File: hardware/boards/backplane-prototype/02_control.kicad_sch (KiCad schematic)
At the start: 13 parts, among them J10 TC2030-IDC-NL SWD, U1 STM32C092GCU6

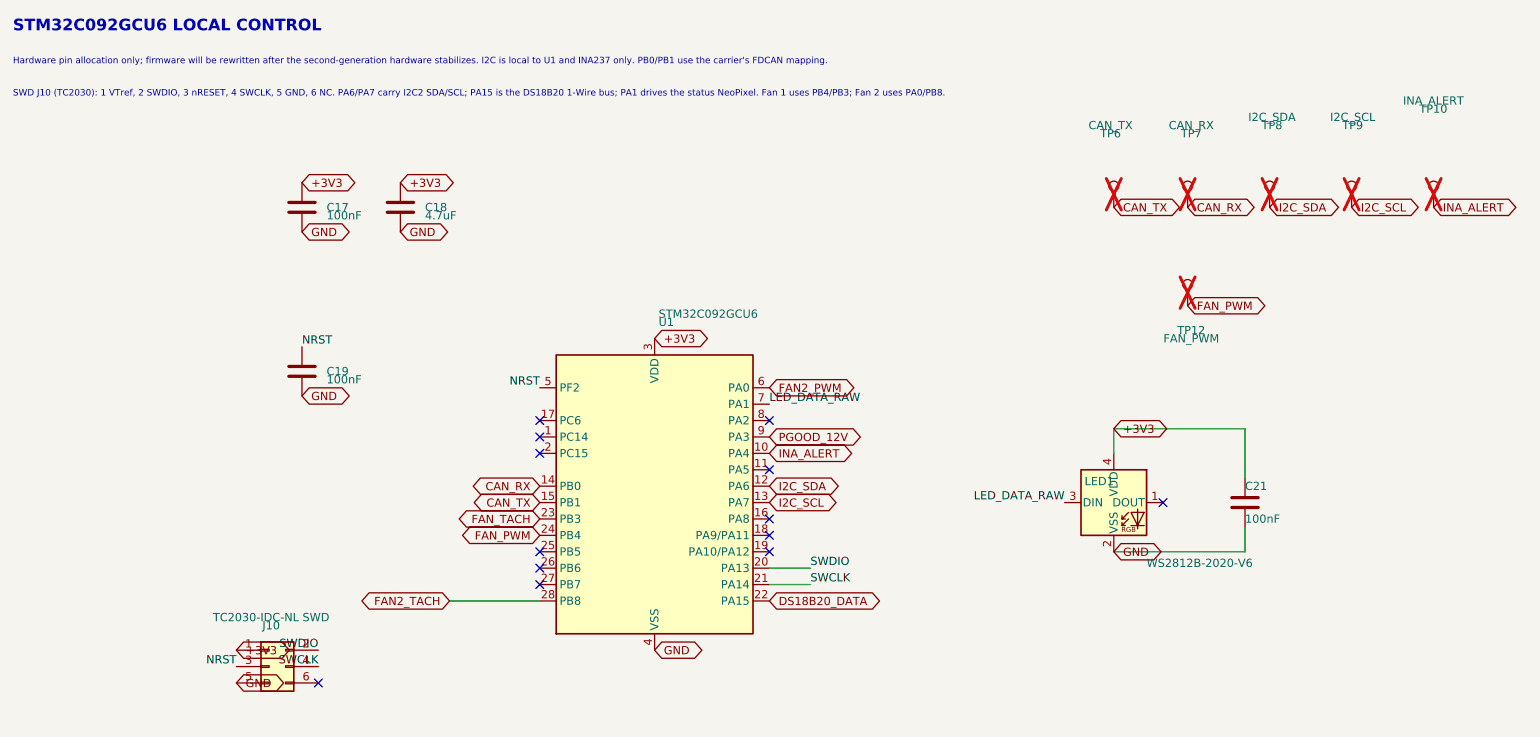
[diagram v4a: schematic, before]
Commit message: move fan1 signals off TIM3 pins
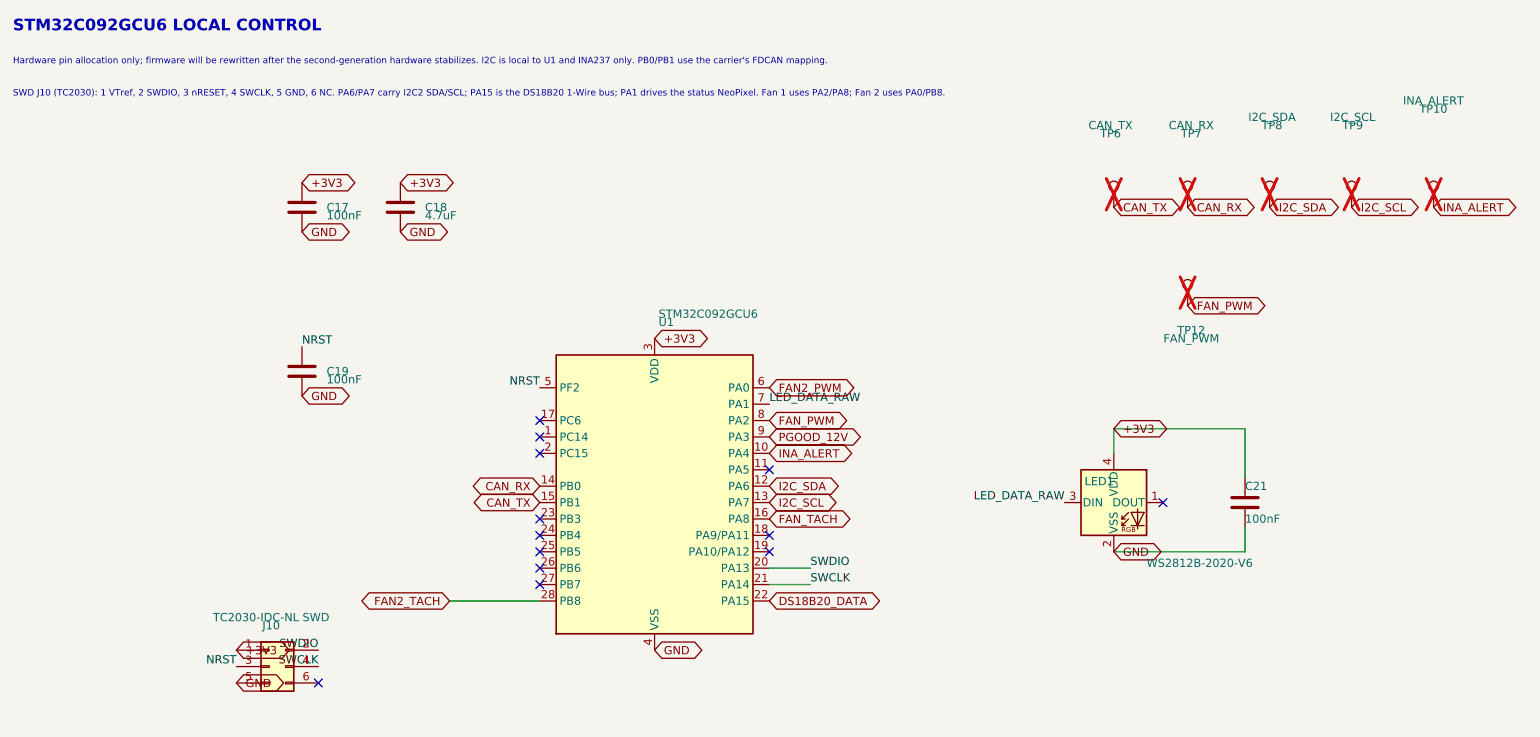
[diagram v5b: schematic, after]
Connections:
- net FAN_PWM: now also U1.8 (PA2); no longer U1.24 (PB4)
- net FAN_TACH: now also U1.16 (PA8); no longer U1.23 (PB3)
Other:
- note added: "SWD J10 (TC2030): 1 VTref, 2 SWDIO, 3 nRESET, 4 SWCLK, 5 GND, 6 NC. PA6/PA7 carry I2C2 SDA/SCL; PA15 is the DS18B20 1-Wire bus; PA1 drives the status NeoPixel. Fan 1 uses PA2/PA8; Fan 2 uses PA0/PB8."
- note removed: "SWD J10 (TC2030): 1 VTref, 2 SWDIO, 3 nRESET, 4 SWCLK, 5 GND, 6 NC. PA6/PA7 carry I2C2 SDA/SCL; PA15 is the DS18B20 1-Wire bus; PA1 drives the status NeoPixel. Fan 1 uses PB4/PB3; Fan 2 uses PA0/PB8."
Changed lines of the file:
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@@
 	(generator_version "10.0")
 	(paper "A4")
-	(text "SWD J10 (TC2030): 1 VTref, 2 SWDIO, 3 nRESET, 4 SWCLK, 5 GND, 6 NC. PA6/PA7 carry I2C2 SDA/SCL; PA15 is the DS18B20 1-Wire bus; PA1 drives the status NeoPixel. Fan 1 uses PB4/PB3; Fan 2 uses PA0/PB8."
+	(text "SWD J10 (TC2030): 1 VTref, 2 SWDIO, 3 nRESET, 4 SWCLK, 5 GND, 6 NC. PA6/PA7 carry I2C2 SDA/SCL; PA15 is the DS18B20 1-Wire bus; PA1 drives the status NeoPixel. Fan 1 uses PA2/PA8; Fan 2 uses PA0/PB8."
 		(exclude_from_sim no)
 		(at 20 27.5 0)
@@
 	)
 	(no_connect
-		(at 137.16 77.47)
+		(at 101.6 95.25)
 	)
 	(no_connect
@@
 	)
 	(no_connect
-		(at 137.16 92.71)
+		(at 101.6 92.71)
 	)
 	(wire
@@
 	(global_label "FAN_TACH"
 		(shape bidirectional)
-		(at 101.6 92.71 180)
+		(at 137.16 92.71 0)
+		(effects
+			(font
+				(size 1.27 1.27)
+			)
+			(justify left)
+		)
+		(property "Intersheetrefs" "${INTERSHEET_REFS}"
+			(at 137.16 92.71 0)
+			(hide yes)
+			(show_name no)
+			(do_not_autoplace no)
+			(effects
+				(font
+					(size 1.27 1.27)
+				)
+			)
+		)
+	)
+	(global_label "+3V3"
+		(shape bidirectional)
+		(at 119.38 64.77 0)
+		(effects
+			(font
+				(size 1.27 1.27)
+			)
+			(justify left)
+		)
+		(property "Intersheetrefs" "${INTERSHEET_REFS}"
+			(at 119.38 64.77 0)
+			(hide yes)
+			(show_name no)
+			(do_not_autoplace no)
+			(effects
+				(font
+					(size 1.27 1.27)
+				)
+			)
+		)
+	)
+	(global_label "I2C_SCL"
+		(shape bidirectional)
+		(at 137.16 90.17 0)
+		(effects
+			(font
+				(size 1.27 1.27)
+			)
+			(justify left)
+		)
+		(property "Intersheetrefs" "${INTERSHEET_REFS}"
+			(at 137.16 90.17 0)
+			(hide yes)
+			(show_name no)
+			(do_not_autoplace no)
+			(effects
+				(font
+					(size 1.27 1.27)
+				)
+			)
+		)
+	)
+	(global_label "CAN_TX"
+		(shape bidirectional)
+		(at 190.5 44.45 0)
+		(effects
+			(font
+				(size 1.27 1.27)
+			)
+			(justify left)
+		)
+		(property "Intersheetrefs" "${INTERSHEET_REFS}"
+			(at 190.5 44.45 0)
+			(hide yes)
+			(show_name no)
+			(do_not_autoplace no)
+			(effects
+				(font
+					(size 1.27 1.27)
+				)
+			)
+		)
+	)
+	(global_label "I2C_SDA"
+		(shape bidirectional)
+		(at 137.16 87.63 0)
+		(effects
+			(font
+				(size 1.27 1.27)
+			)
+			(justify left)
+		)
+		(property "Intersheetrefs" "${INTERSHEET_REFS}"
+			(at 137.16 87.63 0)
+			(hide yes)
+			(show_name no)
+			(do_not_autoplace no)
+			(effects
+				(font
+					(size 1.27 1.27)
+				)
+			)
+		)
+	)
+	(global_label "GND"
+		(shape bidirectional)
+		(at 119.38 113.03 0)
+		(effects
+			(font
+				(size 1.27 1.27)
+			)
+			(justify left)
+		)
+		(property "Intersheetrefs" "${INTERSHEET_REFS}"
+			(at 119.38 113.03 0)
+			(hide yes)
+			(show_name no)
+			(do_not_autoplace no)
+			(effects
+				(font
+					(size 1.27 1.27)
+				)
+			)
+		)
+	)
+	(global_label "+3V3"
+		(shape bidirectional)
+		(at 190.5 78.74 0)
+		(effects
+			(font
+				(size 1.27 1.27)
+			)
+			(justify left)
+		)
+		(property "Intersheetrefs" "${INTERSHEET_REFS}"
+			(at 190.5 78.74 0)
+			(hide yes)
+			(show_name no)
+			(do_not_autoplace no)
+			(effects
+				(font
+					(size 1.27 1.27)
+				)
+			)
+		)
+	)
+	(global_label "GND"
+		(shape bidirectional)
+		(at 64.77 73.66 0)
+		(effects
+			(font
+				(size 1.27 1.27)
+			)
+			(justify left)
+		)
+		(property "Intersheetrefs" "${INTERSHEET_REFS}"
+			(at 64.77 73.66 0)
+			(hide yes)
+			(show_name no)
+			(do_not_autoplace no)
+			(effects
+				(font
+					(size 1.27 1.27)
+				)
+			)
+		)
+	)
+	(global_label "CAN_RX"
+		(shape bidirectional)
+		(at 101.6 87.63 180)
 		(effects
 			(font
@@
 		)
 		(property "Intersheetrefs" "${INTERSHEET_REFS}"
-			(at 101.6 92.71 0)
-			(hide yes)
-			(show_name no)
-			(do_not_autoplace no)
-			(effects
-				(font
-					(size 1.27 1.27)
-				)
-			)
-		)
-	)
-	(global_label "+3V3"
-		(shape bidirectional)
-		(at 119.38 64.77 0)
-		(effects
-			(font
-				(size 1.27 1.27)
-			)
-			(justify left)
-		)
-		(property "Intersheetrefs" "${INTERSHEET_REFS}"
-			(at 119.38 64.77 0)
-			(hide yes)
-			(show_name no)
-			(do_not_autoplace no)
-			(effects
-				(font
-					(size 1.27 1.27)
-				)
-			)
-		)
-	)
-	(global_label "I2C_SCL"
-		(shape bidirectional)
-		(at 137.16 90.17 0)
-		(effects
-			(font
-				(size 1.27 1.27)
-			)
-			(justify left)
-		)
-		(property "Intersheetrefs" "${INTERSHEET_REFS}"
-			(at 137.16 90.17 0)
-			(hide yes)
-			(show_name no)
-			(do_not_autoplace no)
-			(effects
-				(font
-					(size 1.27 1.27)
-				)
-			)
-		)
-	)
-	(global_label "CAN_TX"
-		(shape bidirectional)
-		(at 190.5 44.45 0)
-		(effects
-			(font
-				(size 1.27 1.27)
-			)
-			(justify left)
-		)
-		(property "Intersheetrefs" "${INTERSHEET_REFS}"
-			(at 190.5 44.45 0)
-			(hide yes)
-			(show_name no)
-			(do_not_autoplace no)
-			(effects
-				(font
-					(size 1.27 1.27)
-				)
-			)
-		)
-	)
-	(global_label "I2C_SDA"
-		(shape bidirectional)
-		(at 137.16 87.63 0)
-		(effects
-			(font
-				(size 1.27 1.27)
-			)
-			(justify left)
-		)
-		(property "Intersheetrefs" "${INTERSHEET_REFS}"
-			(at 137.16 87.63 0)
-			(hide yes)
-			(show_name no)
-			(do_not_autoplace no)
-			(effects
-				(font
-					(size 1.27 1.27)
-				)
-			)
-		)
-	)
-	(global_label "GND"
-		(shape bidirectional)
-		(at 119.38 113.03 0)
-		(effects
-			(font
-				(size 1.27 1.27)
-			)
-			(justify left)
-		)
-		(property "Intersheetrefs" "${INTERSHEET_REFS}"
-			(at 119.38 113.03 0)
-			(hide yes)
-			(show_name no)
-			(do_not_autoplace no)
-			(effects
-				(font
-					(size 1.27 1.27)
-				)
-			)
-		)
-	)
-	(global_label "+3V3"
-		(shape bidirectional)
-		(at 190.5 78.74 0)
-		(effects
-			(font
-				(size 1.27 1.27)
-			)
-			(justify left)
-		)
-		(property "Intersheetrefs" "${INTERSHEET_REFS}"
-			(at 190.5 78.74 0)
-			(hide yes)
-			(show_name no)
-			(do_not_autoplace no)
-			(effects
-				(font
-					(size 1.27 1.27)
-				)
-			)
-		)
-	)
-	(global_label "GND"
-		(shape bidirectional)
-		(at 64.77 73.66 0)
-		(effects
-			(font
-				(size 1.27 1.27)
-			)
-			(justify left)
-		)
-		(property "Intersheetrefs" "${INTERSHEET_REFS}"
-			(at 64.77 73.66 0)
-			(hide yes)
-			(show_name no)
-			(do_not_autoplace no)
-			(effects
-				(font
-					(size 1.27 1.27)
-				)
-			)
-		)
-	)
-	(global_label "CAN_RX"
-		(shape bidirectional)
-		(at 101.6 87.63 180)
-		(effects
-			(font
-				(size 1.27 1.27)
-			)
-			(justify right)
-		)
-		(property "Intersheetrefs" "${INTERSHEET_REFS}"
 			(at 101.6 87.63 0)
 			(hide yes)
@@
 	(global_label "FAN_PWM"
 		(shape bidirectional)
-		(at 101.6 95.25 180)
-		(effects
-			(font
-				(size 1.27 1.27)
-			)
-			(justify right)
-		)
-		(property "Intersheetrefs" "${INTERSHEET_REFS}"
-			(at 101.6 95.25 0)
-			(hide yes)
-			(show_name no)
+		(at 137.16 77.47 0)
+		(effects
+			(font
+				(size 1.27 1.27)
+			)
+			(justify left)
+		)
+		(property "Intersheetrefs" "${INTERSHEET_REFS}"
+			(at 137.16 77.47 0)
+			(hide yes)
+			(show_name no)

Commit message: use official KiCad power symbols throughout backplane
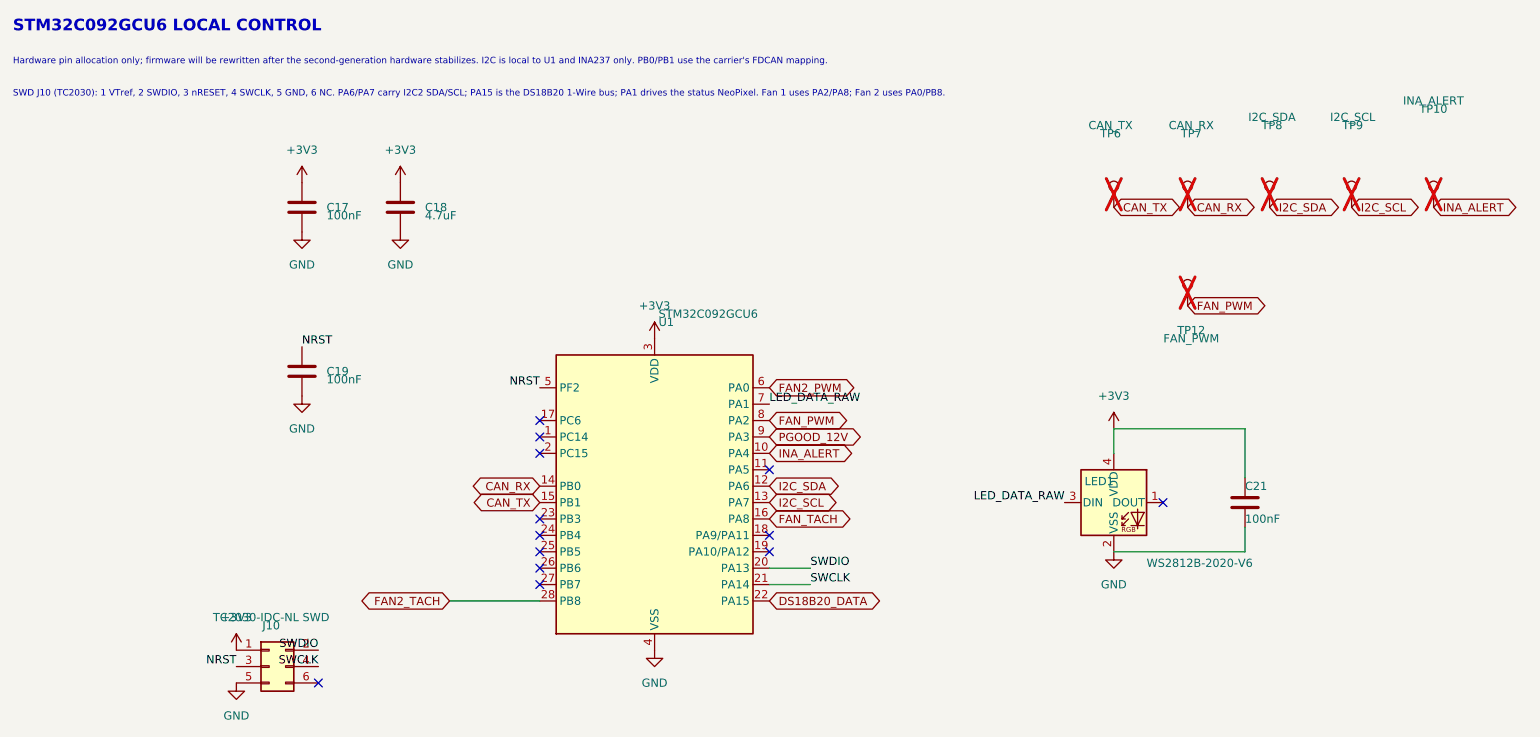
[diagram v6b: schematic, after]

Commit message: swap fan tach inputs
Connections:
- net FAN2_TACH: now also U1.16 (PA8); no longer U1.28 (PB8)
- net FAN_TACH: now also U1.28 (PB8); no longer U1.16 (PA8)
